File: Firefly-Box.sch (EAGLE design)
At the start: 40 parts, among them U1 ATMEGA32U4-XUMU, U2 ATMEGA32U4-XUAU, Y1 16MHz KX-7

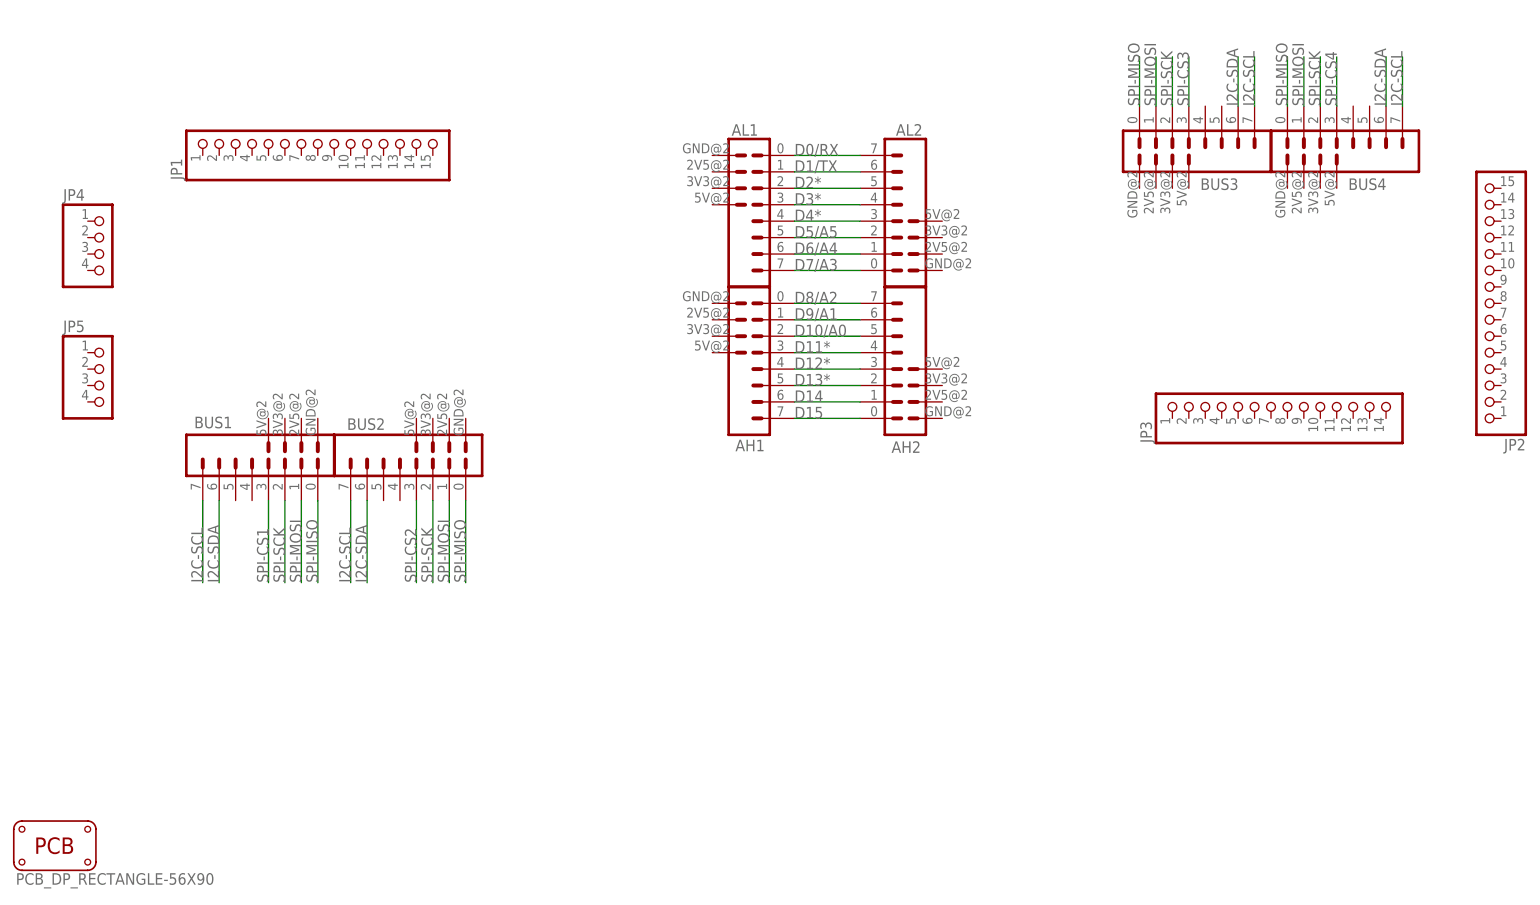
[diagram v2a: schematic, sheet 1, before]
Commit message: Add power to wings
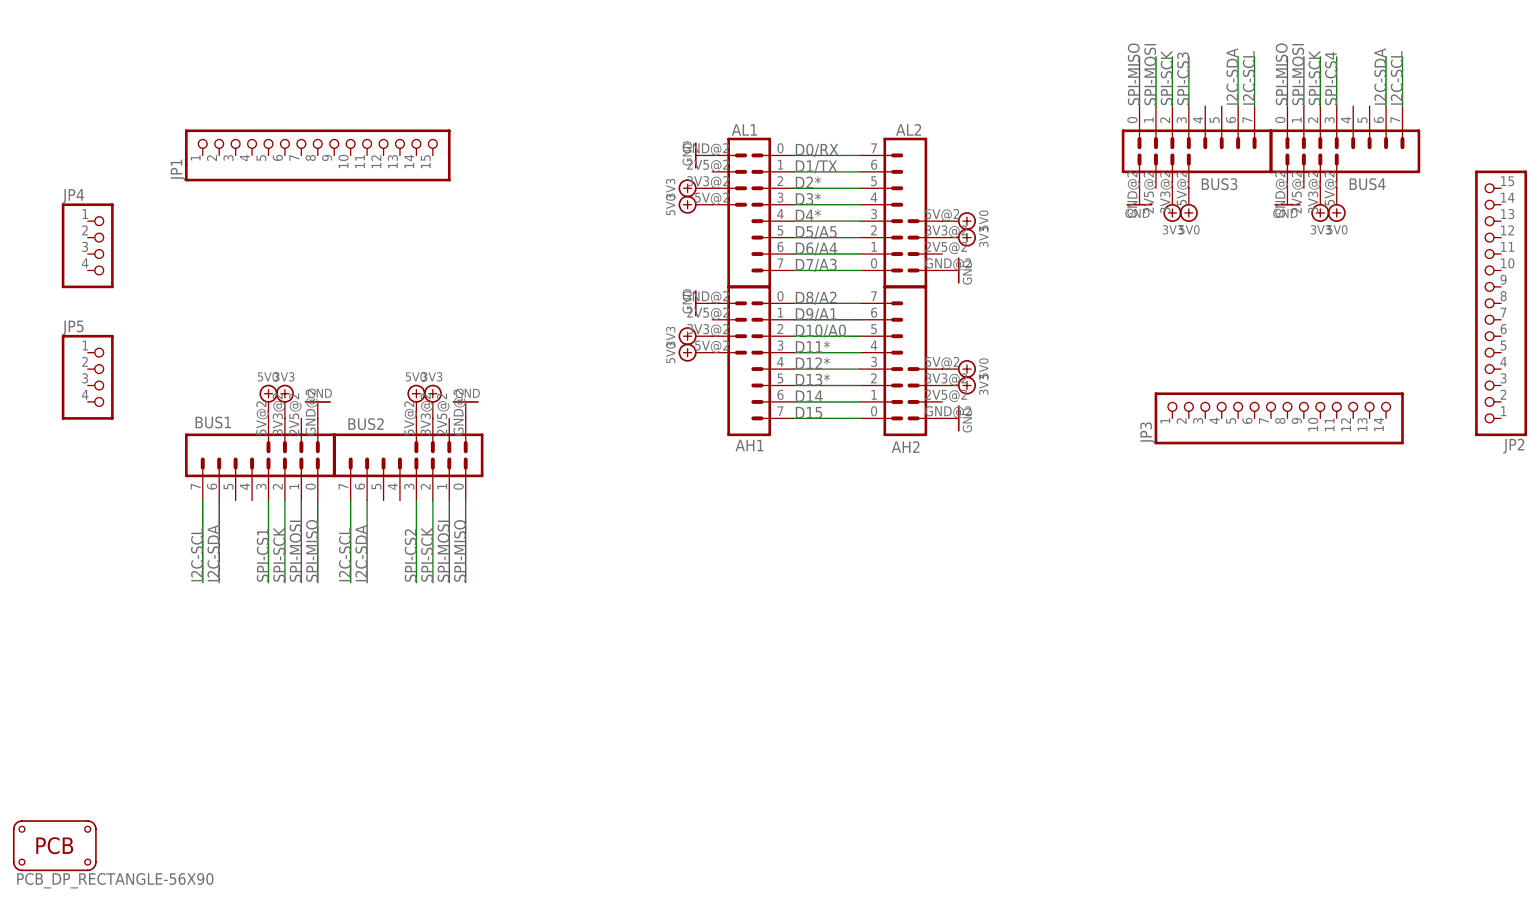
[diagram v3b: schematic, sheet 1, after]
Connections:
- removed net 5V: CONN2USB.VUSB, U1.VBUS
- new net 5V0: AH1.5V, AH2.5V, AL1.5V, AL2.5V, BUS1.5V, BUS2.5V, BUS3.5V, BUS4.5V, CONN2USB.VUSB, U1.VBUS
- net 3V3: now also AH1.3V3, AH2.3V3, AL1.3V3, AL2.3V3, BUS1.3V3, BUS2.3V3, BUS3.3V3, BUS4.3V3
- net GND: now also AH1.GND, AH2.GND, AL1.GND, AL2.GND, BUS1.GND, BUS2.GND, BUS3.GND, BUS4.GND
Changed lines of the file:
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@@
 <part name="JP4" library="pinhead" deviceset="PINHD-1X4" device=""/>
 <part name="JP5" library="pinhead" deviceset="PINHD-1X4" device=""/>
+<part name="GND1" library="GadgetFactory" deviceset="GND" device=""/>
+<part name="GND5" library="GadgetFactory" deviceset="GND" device=""/>
+<part name="GND6" library="GadgetFactory" deviceset="GND" device=""/>
+<part name="GND7" library="GadgetFactory" deviceset="GND" device=""/>
+<part name="GND8" library="GadgetFactory" deviceset="GND" device=""/>
+<part name="GND9" library="GadgetFactory" deviceset="GND" device=""/>
+<part name="GND10" library="GadgetFactory" deviceset="GND" device=""/>
+<part name="GND11" library="GadgetFactory" deviceset="GND" device=""/>
+<part name="3V3_PWR5" library="GadgetFactory" deviceset="3V3" device=""/>
+<part name="3V3_PWR6" library="GadgetFactory" deviceset="3V3" device=""/>
+<part name="3V3_PWR7" library="GadgetFactory" deviceset="3V3" device=""/>
+<part name="3V3_PWR8" library="GadgetFactory" deviceset="3V3" device=""/>
+<part name="3V3_PWR9" library="GadgetFactory" deviceset="3V3" device=""/>
+<part name="3V3_PWR10" library="GadgetFactory" deviceset="3V3" device=""/>
+<part name="3V3_PWR11" library="GadgetFactory" deviceset="3V3" device=""/>
+<part name="3V3_PWR12" library="GadgetFactory" deviceset="3V3" device=""/>
+<part name="5V0_PWR1" library="GadgetFactory" deviceset="5V0" device=""/>
+<part name="5V0_PWR2" library="GadgetFactory" deviceset="5V0" device=""/>
+<part name="5V0_PWR3" library="GadgetFactory" deviceset="5V0" device=""/>
+<part name="5V0_PWR4" library="GadgetFactory" deviceset="5V0" device=""/>
+<part name="5V0_PWR5" library="GadgetFactory" deviceset="5V0" device=""/>
+<part name="5V0_PWR6" library="GadgetFactory" deviceset="5V0" device=""/>
+<part name="5V0_PWR7" library="GadgetFactory" deviceset="5V0" device=""/>
+<part name="5V0_PWR8" library="GadgetFactory" deviceset="5V0" device=""/>
+<part name="5V0_PWR9" library="GadgetFactory" deviceset="5V0" device=""/>
+<part name="5V0_PWR10" library="GadgetFactory" deviceset="5V0" device=""/>
 </parts>
 <sheets>
@@
 <instance part="JP4" gate="A" x="22.86" y="104.14"/>
 <instance part="JP5" gate="A" x="22.86" y="83.82"/>
+<instance part="GND1" gate="A" x="114.3" y="96.52" rot="R270"/>
+<instance part="GND5" gate="A" x="114.3" y="119.38" rot="R270"/>
+<instance part="GND6" gate="A" x="154.94" y="101.6" rot="R90"/>
+<instance part="GND7" gate="A" x="154.94" y="78.74" rot="R90"/>
+<instance part="GND8" gate="A" x="78.74" y="81.28" rot="R180"/>
+<instance part="GND9" gate="A" x="55.88" y="81.28" rot="R180"/>
+<instance part="GND10" gate="A" x="182.88" y="111.76"/>
+<instance part="GND11" gate="A" x="205.74" y="111.76"/>
+<instance part="3V3_PWR5" gate="A" x="50.8" y="81.28"/>
+<instance part="3V3_PWR6" gate="A" x="73.66" y="81.28"/>
+<instance part="3V3_PWR7" gate="A" x="187.96" y="111.76" rot="R180"/>
+<instance part="3V3_PWR8" gate="A" x="210.82" y="111.76" rot="R180"/>
+<instance part="3V3_PWR9" gate="A" x="154.94" y="106.68" rot="R270"/>
+<instance part="3V3_PWR10" gate="A" x="154.94" y="83.82" rot="R270"/>
+<instance part="3V3_PWR11" gate="A" x="114.3" y="114.3" rot="R90"/>
+<instance part="3V3_PWR12" gate="A" x="114.3" y="91.44" rot="R90"/>
+<instance part="5V0_PWR1" gate="A" x="154.94" y="86.36" rot="R270"/>
+<instance part="5V0_PWR2" gate="A" x="154.94" y="109.22" rot="R270"/>
+<instance part="5V0_PWR3" gate="A" x="114.3" y="111.76" rot="R90"/>
+<instance part="5V0_PWR4" gate="A" x="114.3" y="88.9" rot="R90"/>
+<instance part="5V0_PWR5" gate="A" x="190.5" y="111.76" rot="R180"/>
+<instance part="5V0_PWR6" gate="A" x="213.36" y="111.76" rot="R180"/>
+<instance part="5V0_PWR7" gate="A" x="71.12" y="81.28"/>
+<instance part="5V0_PWR8" gate="A" x="48.26" y="81.28"/>
 </instances>
 <busses>
@@
 <wire x1="129.54" y1="88.9" x2="139.7" y2="88.9" width="0.2032" layer="91"/>
 <label x="129.54" y="88.9" size="1.778" layer="95"/>
+</segment>
+</net>
+<net name="GND" class="2">
+<segment>
+<pinref part="AH1" gate="G$1" pin="GND"/>
+<pinref part="GND1" gate="A" pin="GND"/>
+</segment>
+<segment>
+<pinref part="AL1" gate="G$1" pin="GND"/>
+<pinref part="GND5" gate="A" pin="GND"/>
+</segment>
+<segment>
+<pinref part="AL2" gate="G$1" pin="GND"/>
+<pinref part="GND6" gate="A" pin="GND"/>
+</segment>
+<segment>
+<pinref part="AH2" gate="G$1" pin="GND"/>
+<pinref part="GND7" gate="A" pin="GND"/>
+</segment>
+<segment>
+<pinref part="BUS2" gate="G$1" pin="GND"/>
+<pinref part="GND8" gate="A" pin="GND"/>
+</segment>
+<segment>
+<pinref part="BUS1" gate="G$1" pin="GND"/>
+<pinref part="GND9" gate="A" pin="GND"/>
+</segment>
+<segment>
+<pinref part="BUS3" gate="G$1" pin="GND"/>
+<pinref part="GND10" gate="A" pin="GND"/>
+</segment>
+<segment>
+<pinref part="BUS4" gate="G$1" pin="GND"/>
+<pinref part="GND11" gate="A" pin="GND"/>
+</segment>
+</net>
+<net name="3V3" class="0">
+<segment>
+<pinref part="BUS1" gate="G$1" pin="3V3"/>
+<pinref part="3V3_PWR5" gate="A" pin="3V3"/>
+</segment>
+<segment>
+<pinref part="BUS2" gate="G$1" pin="3V3"/>
+<pinref part="3V3_PWR6" gate="A" pin="3V3"/>
+</segment>
+<segment>
+<pinref part="BUS3" gate="G$1" pin="3V3"/>
+<pinref part="3V3_PWR7" gate="A" pin="3V3"/>
+</segment>
+<segment>
+<pinref part="BUS4" gate="G$1" pin="3V3"/>
+<pinref part="3V3_PWR8" gate="A" pin="3V3"/>
+</segment>
+<segment>
+<pinref part="AL2" gate="G$1" pin="3V3"/>
+<pinref part="3V3_PWR9" gate="A" pin="3V3"/>
+</segment>
+<segment>
+<pinref part="AH2" gate="G$1" pin="3V3"/>
+<pinref part="3V3_PWR10" gate="A" pin="3V3"/>
+</segment>
+<segment>
+<pinref part="AL1" gate="G$1" pin="3V3"/>
+<pinref part="3V3_PWR11" gate="A" pin="3V3"/>
+</segment>
+<segment>
+<pinref part="AH1" gate="G$1" pin="3V3"/>
+<pinref part="3V3_PWR12" gate="A" pin="3V3"/>
+</segment>
+</net>
+<net name="5V0" class="0">
+<segment>
+<pinref part="AH2" gate="G$1" pin="5V"/>
+<pinref part="5V0_PWR1" gate="A" pin="5V0"/>
+</segment>
+<segment>
+<pinref part="AL2" gate="G$1" pin="5V"/>
+<pinref part="5V0_PWR2" gate="A" pin="5V0"/>
+</segment>
+<segment>
+<pinref part="AL1" gate="G$1" pin="5V"/>
+<pinref part="5V0_PWR3" gate="A" pin="5V0"/>
+</segment>
+<segment>
+<pinref part="AH1" gate="G$1" pin="5V"/>
+<pinref part="5V0_PWR4" gate="A" pin="5V0"/>
+</segment>
+<segment>
+<pinref part="BUS3" gate="G$1" pin="5V"/>
+<pinref part="5V0_PWR5" gate="A" pin="5V0"/>
+</segment>
+<segment>
+<pinref part="BUS4" gate="G$1" pin="5V"/>
+<pinref part="5V0_PWR6" gate="A" pin="5V0"/>
+</segment>
+<segment>
+<pinref part="BUS2" gate="G$1" pin="5V"/>
+<pinref part="5V0_PWR7" gate="A" pin="5V0"/>
+</segment>
+<segment>
+<pinref part="BUS1" gate="G$1" pin="5V"/>
+<pinref part="5V0_PWR8" gate="A" pin="5V0"/>
 </segment>
 </net>
@@
 <instance part="R11" gate="A" x="335.28" y="-38.1" rot="R270"/>
 <instance part="CONN2" gate="USB" x="-116.84" y="-2.54"/>
+<instance part="5V0_PWR9" gate="A" x="-81.28" y="2.54"/>
+<instance part="5V0_PWR10" gate="A" x="-38.1" y="66.04"/>
 </instances>
 <busses>
@@
 <label x="142.24" y="73.66" size="1.778" layer="95"/>
 <pinref part="U2" gate="G$1" pin="UGND"/>
-</segment>
-</net>
-<net name="5V" class="3">
-<segment>
-<wire x1="-81.28" y1="0" x2="-81.28" y2="10.16" width="0.1524" layer="91"/>
-<wire x1="-81.28" y1="10.16" x2="-66.04" y2="10.16" width="0.1524" layer="91"/>
-<wire x1="-101.6" y1="0" x2="-81.28" y2="0" width="0.1524" layer="91"/>
-<label x="-91.44" y="0" size="1.778" layer="95" rot="MR0"/>
-<label x="-78.74" y="10.16" size="1.778" layer="95"/>
-<pinref part="CONN2" gate="USB" pin="VUSB"/>
-<wire x1="-101.6" y1="0" x2="-111.76" y2="0" width="0.2032" layer="91"/>
-</segment>
-<segment>
-<wire x1="-7.62" y1="71.12" x2="-27.94" y2="71.12" width="0.1524" layer="91"/>
-<wire x1="-27.94" y1="71.12" x2="-27.94" y2="58.42" width="0.1524" layer="91"/>
-<wire x1="-27.94" y1="58.42" x2="-38.1" y2="58.42" width="0.1524" layer="91"/>
-<wire x1="-38.1" y1="58.42" x2="-38.1" y2="63.5" width="0.1524" layer="91"/>
-<label x="-35.56" y="58.42" size="1.778" layer="95"/>
-<pinref part="U1" gate="G$1" pin="VBUS"/>
 </segment>
 </net>
@@
 </segment>
 </net>
+<net name="5V0" class="0">
+<segment>
+<wire x1="-101.6" y1="0" x2="-81.28" y2="0" width="0.1524" layer="91"/>
+<label x="-91.44" y="0" size="1.778" layer="95" rot="MR0"/>
+<pinref part="CONN2" gate="USB" pin="VUSB"/>
+<wire x1="-101.6" y1="0" x2="-111.76" y2="0" width="0.2032" layer="91"/>
+<pinref part="5V0_PWR9" gate="A" pin="5V0"/>
+</segment>
+<segment>
+<wire x1="-7.62" y1="71.12" x2="-27.94" y2="71.12" width="0.1524" layer="91"/>
+<wire x1="-27.94" y1="71.12" x2="-27.94" y2="58.42" width="0.1524" layer="91"/>
+<wire x1="-27.94" y1="58.42" x2="-38.1" y2="58.42" width="0.1524" layer="91"/>
+<wire x1="-38.1" y1="58.42" x2="-38.1" y2="63.5" width="0.1524" layer="91"/>
+<label x="-35.56" y="58.42" size="1.778" layer="95"/>
+<pinref part="U1" gate="G$1" pin="VBUS"/>
+<pinref part="5V0_PWR10" gate="A" pin="5V0"/>
+</segment>
+</net>

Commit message: Added Power and LiPo section.
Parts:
- added C10: 4.7uF, SparkFun-Passives:CAP0603-CAP
- added C11, C12: 4.7uF, SparkFun-Passives:CAP1206
- added C8: 470pF, SparkFun-Passives:CAP0603-CAP
- added C9: .1uF, SparkFun-Passives:CAP0603-CAP
- added D1: B340A, SparkFun-DiscreteSemi:DIODE-SCHOTTKY_
- added JP6: JST-2, SparkFun-Connectors:M02-JST-2MM-SMT
- added LED1: RED, SparkFun-LED:LED0603
- added R12: 330, SparkFun-Passives:RESISTOR0603-RES
- added R13: 10k, SparkFun-Passives:RESISTOR0603-RES
- added S1: SWITCH-DPDTSMD, SparkFun-Electromechanical:SWITCH-DPDTSMD
- added U3: MCP73831, SparkFun-PowerIC:MCP73831
- added U4: MIC5219, SparkFun-PowerIC:V_REG_MIC5219SMD
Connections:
- new net N$1: S1.2, U4.EN
- new net N$4: LED1.A, R12.1
- new net N$5: LED1.C, U3.STAT
- new net N$6: R13.2, U3.PROG
- new net N$8: C8.1, U4.BP
- new net V_BATT: C12.2, D1.A, JP6.1, U3.VBAT
- net 3V3: now also C10.2, C9.2, U4.OUT
- net 5V0: now also C11.2, D1.C, R12.2, S1.1, U3.VIN, U4.IN
- net GND: now also C10.1, C11.1, C12.1, C8.2, C9.1, JP6.2, R13.1, S1.3, U3.VSS, U4.GND
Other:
- note added: "10"
- note added: "Battery Input Bypass"
- note added: "Charge Circuit Bypass"
- note added: "L. Buechly and N. Seidle"
- note added: "Lipo Battery section derived from Lilypad USB design."
- note added: "MIC5219 BYPASS"
- note added: "Mike Hord"
- note added: "Original Lilypad Design by:"

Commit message: Lots of routing done.
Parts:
- removed L: Yellow, led:LEDCHIPLED_0805
- removed ON: Green, led:LEDCHIPLED_0805
- removed R10, R11: 1K, GadgetFactory_6.0:R0805
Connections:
- removed net N$2: L.A, R10A.2
- removed net N$3: ON.A, R11A.2
- removed net VUSB: U2.VBUS
- net 3V3: no longer R11A.1
- net 5V0: now also U2.VBUS
- net D11*: now also AH1.6, AH2.3; no longer AH1.4, AH2.5
- net D12*: now also AL1.4, AL2.5; no longer AH1.5, AH2.4
- net D13*: now also AL1.5, AL2.4; no longer AH1.6, AH2.3
- net D3*: now also AH1.5, AH2.4; no longer AL1.4, AL2.5
- net D4*: now also AH1.4, AH2.5; no longer AL1.5, AL2.4, R10A.1
- net GND: no longer L.C, ON.C

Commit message: Fully Routed
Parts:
- removed JP5: (no value), pinhead:PINHD-1X4
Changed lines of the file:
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@@
 <part name="JP3" library="pinhead" deviceset="PINHD-1X14" device=""/>
 <part name="JP4" library="pinhead" deviceset="PINHD-1X4" device=""/>
-<part name="JP5" library="pinhead" deviceset="PINHD-1X4" device=""/>
 <part name="GND1" library="GadgetFactory" deviceset="GND" device=""/>
 <part name="GND5" library="GadgetFactory" deviceset="GND" device=""/>
@@
 <instance part="JP3" gate="A" x="203.2" y="81.28" rot="R90"/>
 <instance part="JP4" gate="A" x="22.86" y="104.14"/>
-<instance part="JP5" gate="A" x="22.86" y="83.82"/>
 <instance part="GND1" gate="A" x="114.3" y="96.52" rot="R270"/>
 <instance part="GND5" gate="A" x="114.3" y="119.38" rot="R270"/>
